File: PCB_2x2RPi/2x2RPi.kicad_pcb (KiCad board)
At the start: 2 copper layers, 44.4 x 53.3 mm, 31 parts, among them K1 RELAY, K2 RELAY, P1 VIN, P2 CONN_13X2, P3 INPUT, P4 Relay1, P6 Relay2, SW1 PWR, U1 LowCurVReg, U2 LowCurVReg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

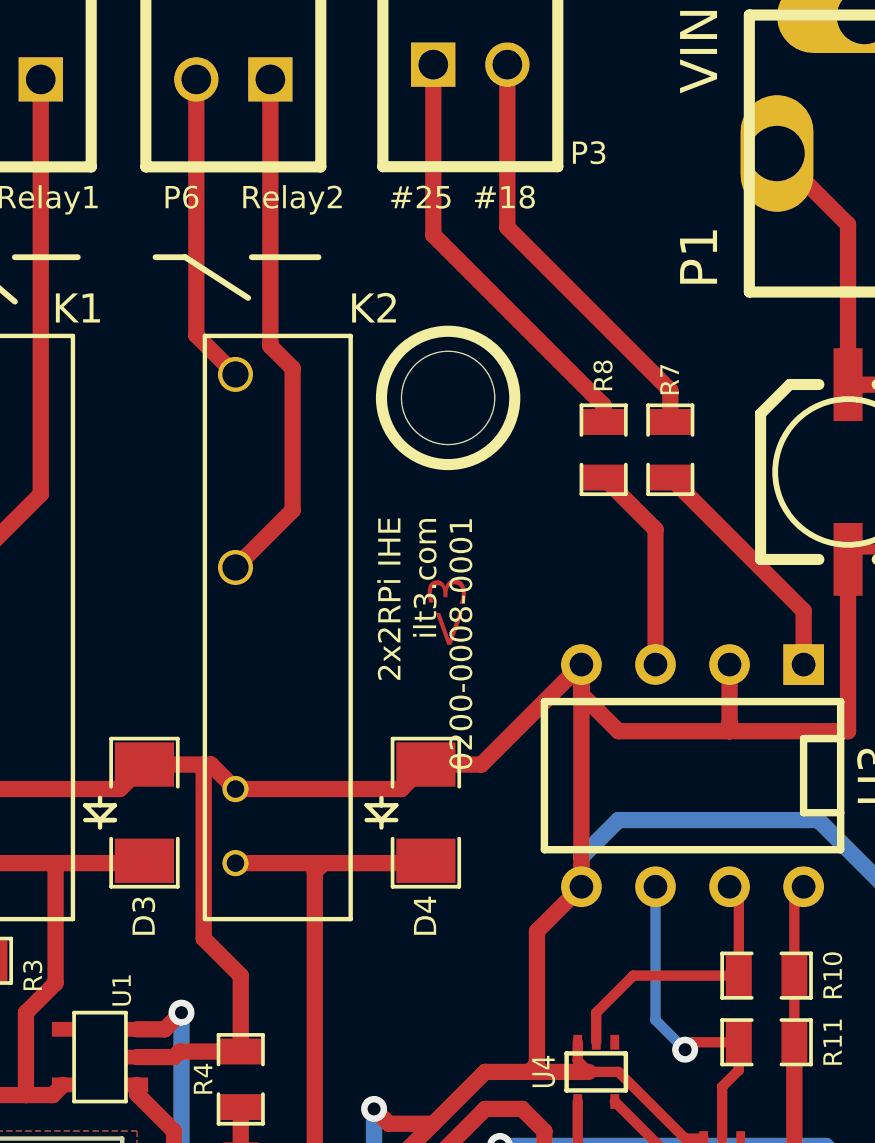
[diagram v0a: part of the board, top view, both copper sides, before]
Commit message: Updated gerber files for 2x2Rpi
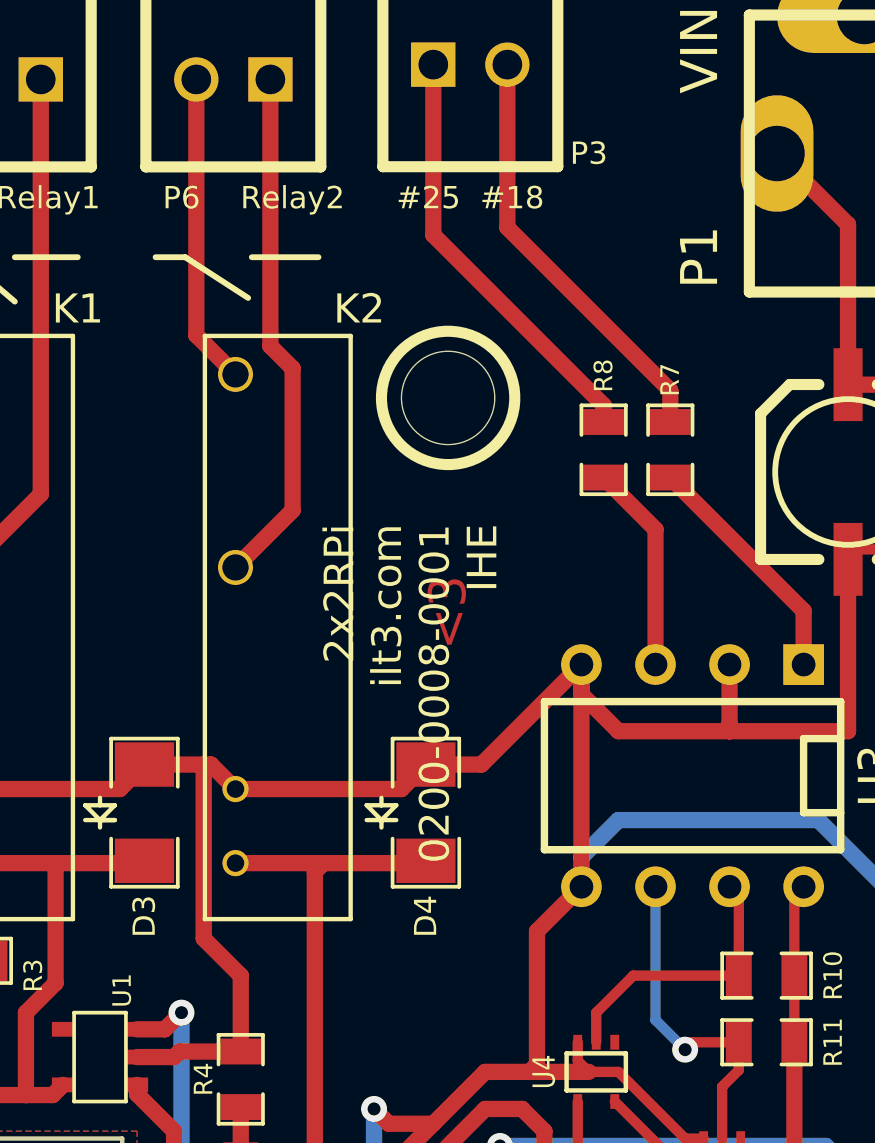
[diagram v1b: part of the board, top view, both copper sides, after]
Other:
- board text added: "2x2RPi ilt3.com 0200-0008-0001 IHE"
- board text removed: "2x2RPi IHE ilt3.com 0200-0008-0001"
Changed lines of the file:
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@@
       (layerselection 283672577)
       (usegerberextensions false)
-      (excludeedgelayer false)
+      (excludeedgelayer true)
       (linewidth 152400)
       (plotframeref false)
@@
       (effects (font (size 0.762 0.762) (thickness 0.1524)))
     )
-    (fp_text user "#25  #18" (at -0.254 4.572) (layer F.SilkS)
+    (fp_text user "#25  #18" (at 0 4.572) (layer F.SilkS)
       (effects (font (size 0.762 0.762) (thickness 0.15)))
     )
@@
   (module Relay (layer F.Cu)
     (at 104.394 72.136 90)
-    (fp_text reference K2 (at 10.922 3.302 180) (layer F.SilkS)
+    (fp_text reference K2 (at 10.922 2.794 180) (layer F.SilkS)
       (effects (font (size 1 1) (thickness 0.15)))
     )
@@
     (arrow2b (pts (xy 93.98 101.6) (xy 93.39358 100.473497)))
   )
-  (gr_text "2x2RPi IHE\nilt3.com\n0200-0008-0001" (at 109.474 68.326 90) (layer F.SilkS)
-    (effects (font (size 0.762 0.762) (thickness 0.1905)) (justify right))
+  (gr_text "2x2RPi\nilt3.com\n0200-0008-0001\nIHE" (at 108.966 68.58 90) (layer F.SilkS)
+    (effects (font (size 1.016 1.016) (thickness 0.1905)) (justify right))
   )
   (gr_line (start 95.377 59.436) (end 97.536 59.436) (angle 90) (layer F.SilkS) (width 0.2))

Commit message: adding 2x2RBee files
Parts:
- P1: value VIN -> 5V reg
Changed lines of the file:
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@@
       (effects (font (thickness 0.3048)))
     )
-    (fp_text value VIN (at 9.144 3.556 270) (layer F.SilkS)
+    (fp_text value "5V reg" (at 9.144 3.556 270) (layer F.SilkS)
       (effects (font (thickness 0.3048)))
     )
@@
   (segment (start 122.428 71.5645) (end 117.856 66.9925) (width 0.5588) (layer F.Cu) (net 34))
   (zone (net 12) (net_name GND) (layer F.Cu) (hatch edge 0.508)
-    (connect_pads yes (clearance 0.508))
+    (connect_pads (clearance 0.508))
     (min_thickness 0.254)
     (fill (arc_segments 16) (thermal_gap 5.08) (thermal_bridge_width 5.08))
@@
   )
   (zone (net 12) (net_name GND) (layer B.Cu) (hatch edge 0.508)
-    (connect_pads yes (clearance 0.508))
+    (connect_pads (clearance 0.508))
     (min_thickness 0.254)
     (fill (arc_segments 16) (thermal_gap 5.08) (thermal_bridge_width 5.08))
